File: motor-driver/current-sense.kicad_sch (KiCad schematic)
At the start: 49 parts, among them U1 LM358DR, U2 LM358DR, U3 LM358DR, U4 LM358DR, U5 LM358DR

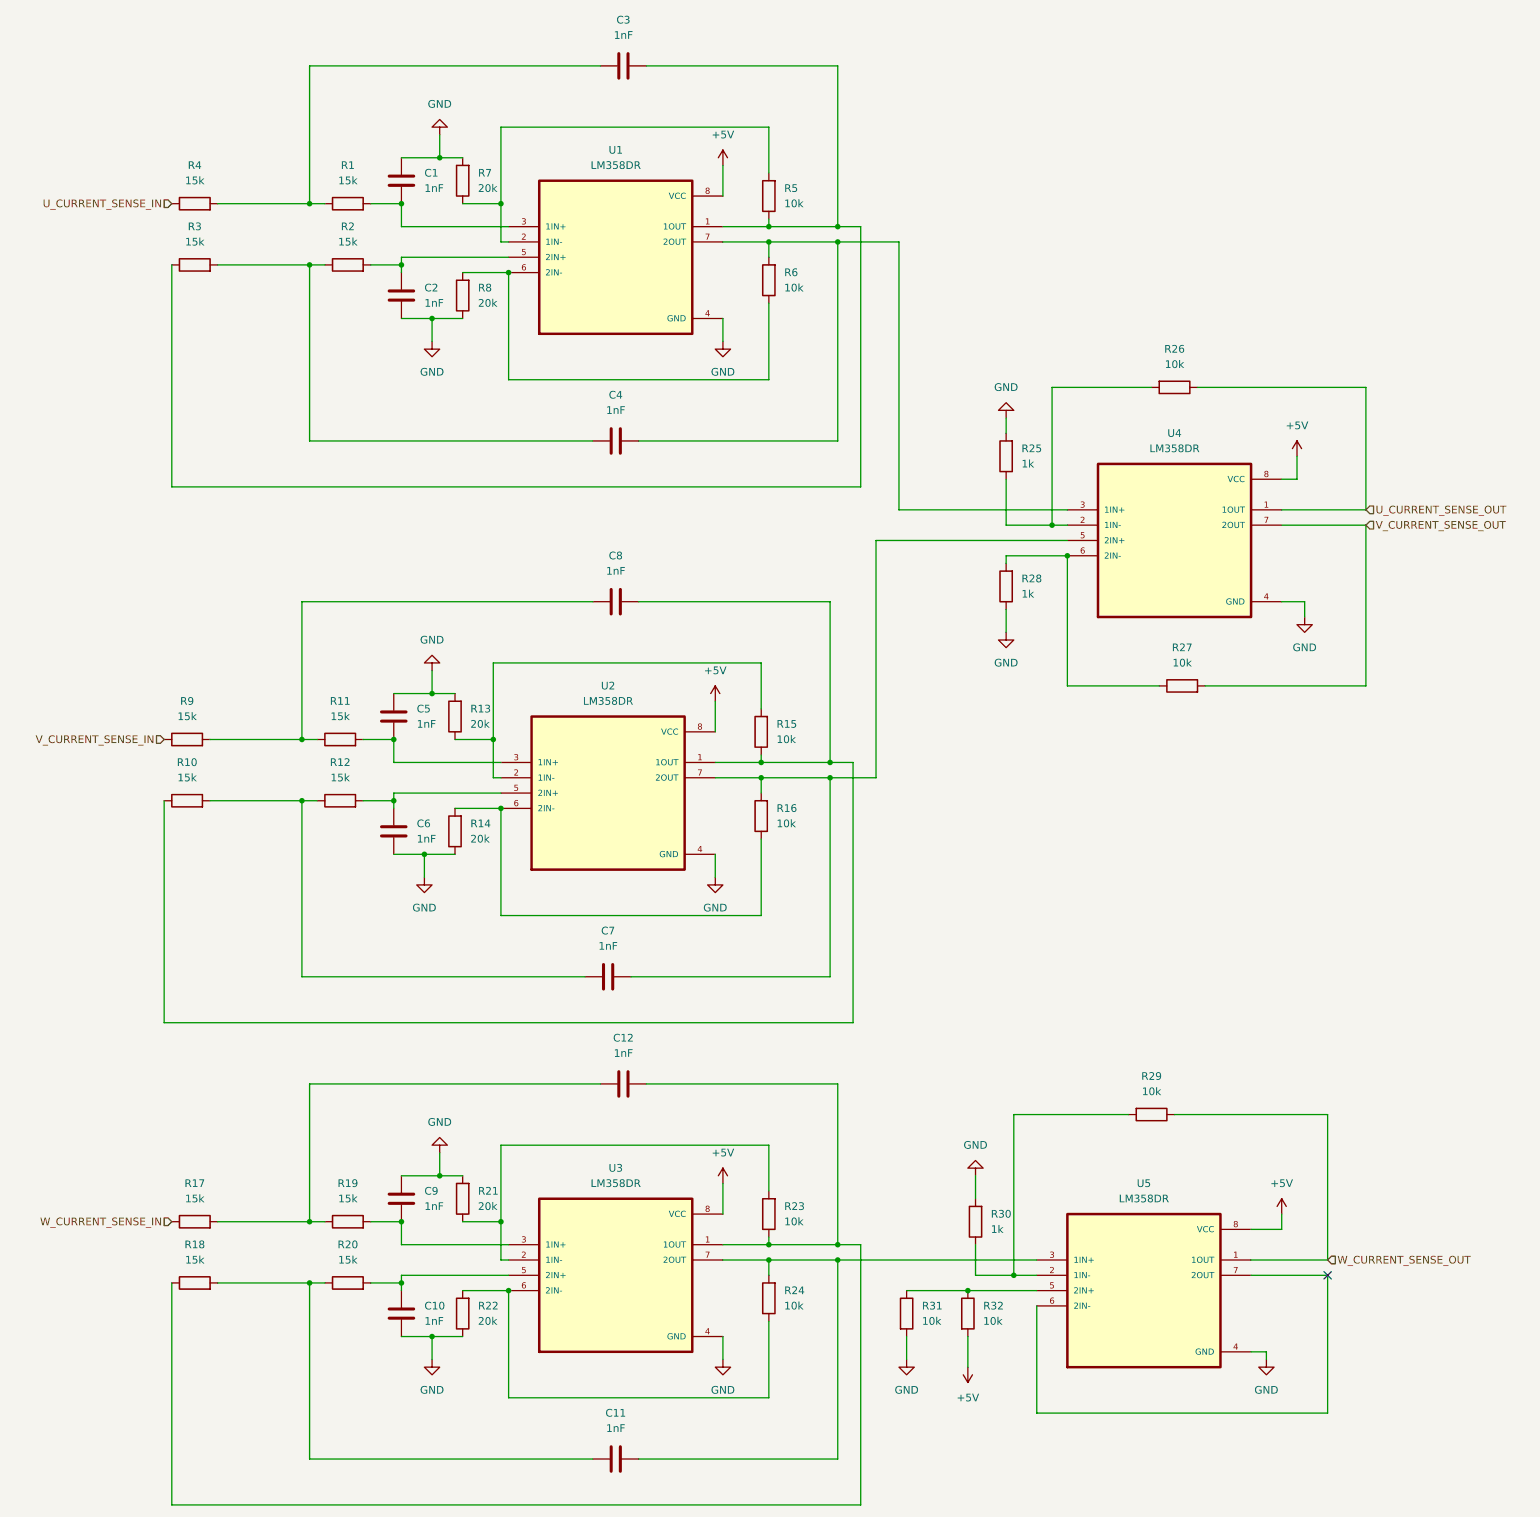
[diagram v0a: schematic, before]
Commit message: completed sheet connections
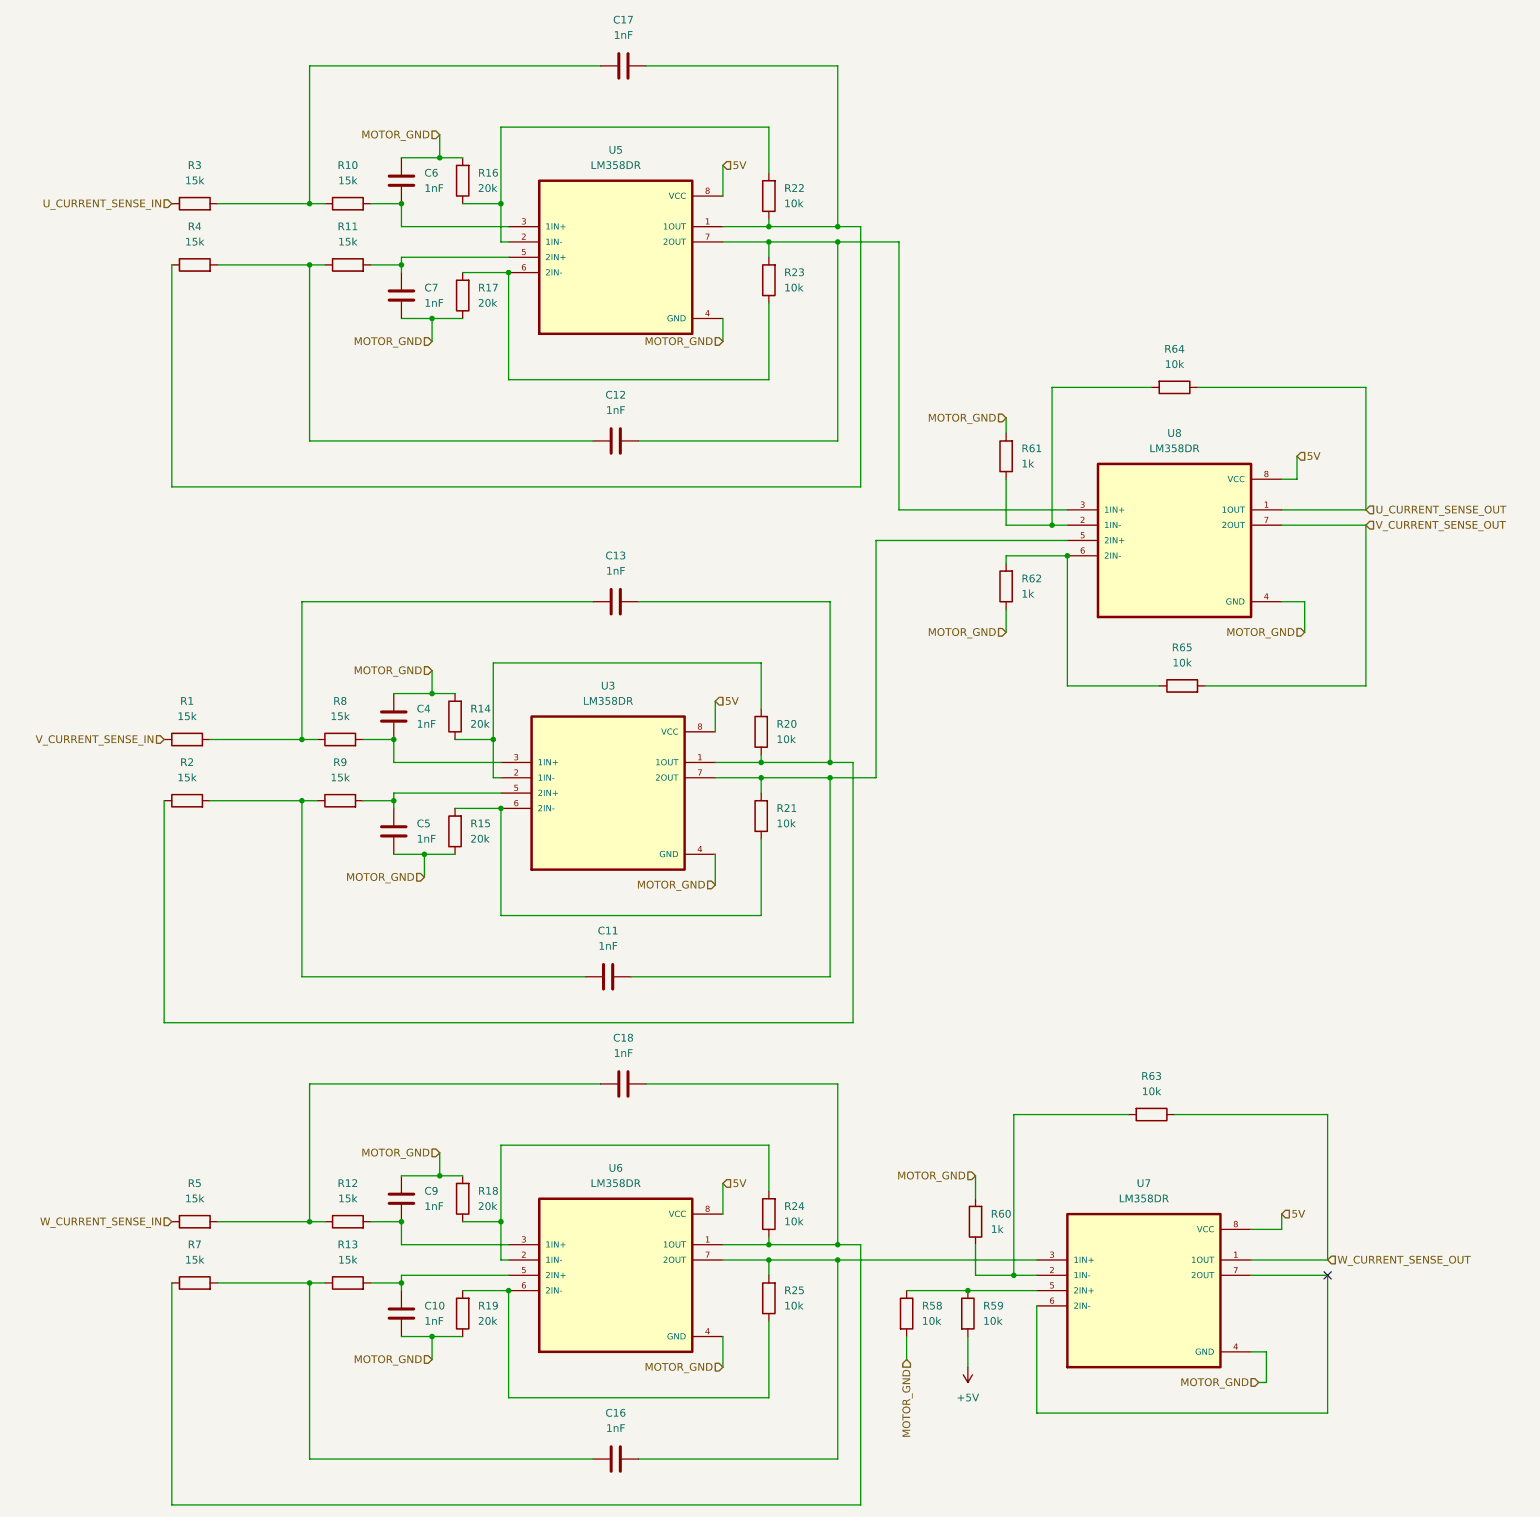
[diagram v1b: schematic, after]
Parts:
- renumbered C7 to C11, C4 to C12, C8 to C13, C11 to C16, C3 to C17, C12 to C18, C5 to C4, C6 to C5, C1 to C6, C2 to C7, R9 to R1, R1 to R10, R2 to R11, R19 to R12, R20 to R13, R13 to R14, R14 to R15, R7 to R16, R8 to R17, R21 to R18, R22 to R19, R10 to R2, R15 to R20, R16 to R21, R5 to R22, R6 to R23, R23 to R24, R24 to R25, R4 to R3, R3 to R4, R17 to R5, R31 to R58, R32 to R59, R30 to R60, R25 to R61, R28 to R62, R29 to R63, R26 to R64, R27 to R65, R18 to R7, R11 to R8, R12 to R9, U2 to U3, U1 to U5, U3 to U6, U5 to U7, U4 to U8
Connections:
- net +5V: no longer U3.8 (VCC), U5.8 (VCC), U6.8 (VCC), U7.8 (VCC), U8.8 (VCC)
- net GND renamed MOTOR_GND
- new net 5V: U3.8 (VCC), U5.8 (VCC), U6.8 (VCC), U7.8 (VCC), U8.8 (VCC)

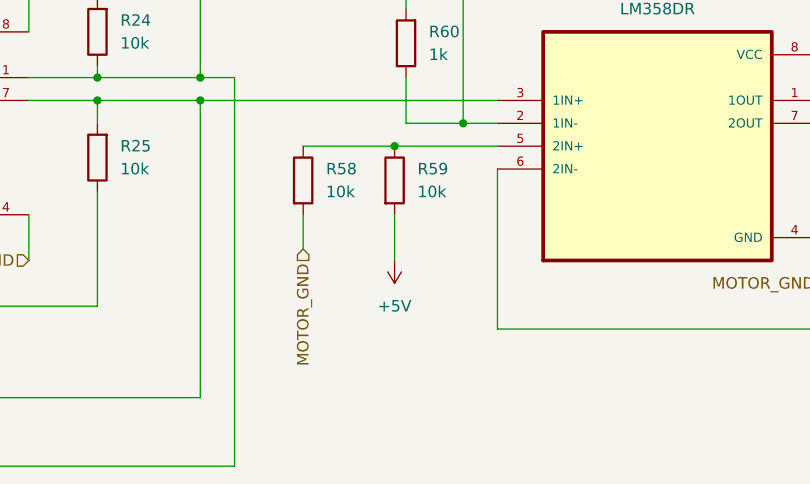
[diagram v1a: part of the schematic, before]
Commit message: added connectors starting pcb layout
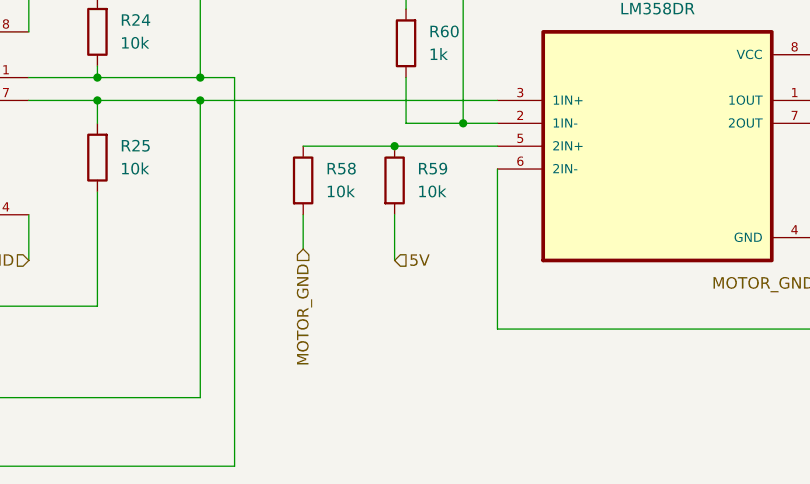
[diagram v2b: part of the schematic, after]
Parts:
- C10, C11, C12, C13, C16, C17, C18, C4, C5, C6, C7, C9: footprint (none) -> Capacitor_SMD:C_0805_2012Metric
- R1, R10, R11, R12, R13, R14, R15, R16, R17, R18, R19, R2, R20, R21, R22, R23, R24, R25, R3, R4, R5, R58, R59, R60, R61, R62, R63, R64, R65, R7, R8, R9: footprint (none) -> Resistor_SMD:R_0805_2012Metric
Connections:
- net +5V is gone; now on net 5V: R59.2
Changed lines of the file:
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@@
 		)
 	)
+	(hierarchical_label "5V"
+		(shape input)
+		(at 176.53 237.49 0)
+		(effects
+			(font
+				(size 1.27 1.27)
+			)
+			(justify left)
+		)
+	)
 	(hierarchical_label "MOTOR_GND"
 		(shape input)
@@
 			)
 		)
-		(property "Footprint" ""
+		(property "Footprint" "Resistor_SMD:R_0805_2012Metric"
 			(at 94.488 40.64 90)
 			(effects
@@
 			)
 		)
-		(property "Footprint" ""
+		(property "Footprint" "Resistor_SMD:R_0805_2012Metric"
 			(at 174.752 228.6 90)
 			(effects
@@
 			)
 		)
-		(property "Footprint" ""
+		(property "Footprint" "Resistor_SMD:R_0805_2012Metric"
 			(at 46.99 145.288 90)
 			(effects
@@
 			)
 		)
-		(property "Footprint" ""
+		(property "Footprint" "Capacitor_SMD:C_0805_2012Metric"
 			(at 115.57 22.5552 0)
 			(effects
@@
 			)
 		)
-		(property "Footprint" ""
+		(property "Footprint" "Resistor_SMD:R_0805_2012Metric"
 			(at 145.288 212.09 90)
 			(effects
@@
 			)
 		)
-		(property "Footprint" ""
+		(property "Footprint" "Capacitor_SMD:C_0805_2012Metric"
 			(at 114.3 111.4552 0)
 			(effects
@@
 			)
 		)
-		(property "Footprint" ""
+		(property "Footprint" "Resistor_SMD:R_0805_2012Metric"
 			(at 145.288 43.18 90)
 			(effects
@@
 			)
 		)
-		(property "Footprint" ""
+		(property "Footprint" "Resistor_SMD:R_0805_2012Metric"
 			(at 164.592 228.6 90)
 			(effects
@@
 			)
 		)
-		(property "Footprint" ""
+		(property "Footprint" "Capacitor_SMD:C_0805_2012Metric"
 			(at 81.5848 55.88 0)
 			(effects
@@
 			)
 		)
-		(property "Footprint" ""
+		(property "Footprint" "Capacitor_SMD:C_0805_2012Metric"
 			(at 80.3148 144.78 0)
 			(effects
@@
 			)
 		)
-		(property "Footprint" ""
+		(property "Footprint" "Resistor_SMD:R_0805_2012Metric"
 			(at 145.288 57.15 90)
 			(effects
@@
 			)
 		)
-		(property "Footprint" ""
+		(property "Footprint" "Resistor_SMD:R_0805_2012Metric"
 			(at 73.66 46.228 90)
 			(effects
@@
 			)
 		)
-		(property "Footprint" ""
+		(property "Footprint" "Capacitor_SMD:C_0805_2012Metric"
 			(at 81.5848 205.74 0)
 			(effects
@@
 			)
 		)
-		(property "Footprint" ""
+		(property "Footprint" "Resistor_SMD:R_0805_2012Metric"
 			(at 48.26 215.138 90)
 			(effects
@@
 			)
 		)
-		(property "Footprint" ""
+		(property "Footprint" "Resistor_SMD:R_0805_2012Metric"
 			(at 210.82 73.152 90)
 			(effects
@@
 			)
 		)
-		(property "Footprint" ""
+		(property "Footprint" "Resistor_SMD:R_0805_2012Metric"
 			(at 46.99 135.128 90)
 			(effects
@@
 			)
 		)
-		(property "Footprint" ""
+		(property "Footprint" "Resistor_SMD:R_0805_2012Metric"
 			(at 73.66 215.138 90)
 			(effects
@@
 			)
 		)
-		(property "Footprint" ""
+		(property "Footprint" "Resistor_SMD:R_0805_2012Metric"
 			(at 48.26 56.388 90)
 			(effects
@@
 			)
 		)
-		(property "Footprint" ""
+		(property "Footprint" "Capacitor_SMD:C_0805_2012Metric"
 			(at 114.3 253.6952 0)
 			(effects
@@
 			)
 		)
-		(property "Footprint" ""
+		(property "Footprint" "Resistor_SMD:R_0805_2012Metric"
 			(at 94.488 228.6 90)
 			(effects
@@
 			)
 		)
-		(property "Footprint" ""
+		(property "Footprint" "Capacitor_SMD:C_0805_2012Metric"
 			(at 115.57 191.4652 0)
 			(effects
@@
 			)
 		)
-		(property "Footprint" ""
+		(property "Footprint" "Resistor_SMD:R_0805_2012Metric"
 			(at 207.01 193.802 90)
 			(effects
@@
 			)
 		)
-		(property "Footprint" ""
+		(property "Footprint" "Capacitor_SMD:C_0805_2012Metric"
 			(at 81.5848 224.79 0)
 			(effects
@@
 			)
 		)
-		(property "Footprint" ""
+		(property "Footprint" "Capacitor_SMD:C_0805_2012Metric"
 			(at 114.3 84.7852 0)
 			(effects
@@
 			)
 		)
-		(property "Footprint" ""
+		(property "Footprint" "Resistor_SMD:R_0805_2012Metric"
 			(at 48.26 225.298 90)
 			(effects
@@
 			)
 		)
-		(property "Footprint" ""
+		(property "Footprint" "Resistor_SMD:R_0805_2012Metric"
 			(at 145.288 226.06 90)
 			(effects
@@
 			)
 		)
-		(property "Footprint" ""
+		(property "Footprint" "Resistor_SMD:R_0805_2012Metric"
 			(at 48.26 46.228 90)
 			(effects
@@
 			)
 		)
-		(property "Footprint" ""
+		(property "Footprint" "Resistor_SMD:R_0805_2012Metric"
 			(at 94.488 59.69 90)
 			(effects
@@
 			)
 		)
-		(property "Footprint" ""
+		(property "Footprint" "Resistor_SMD:R_0805_2012Metric"
 			(at 93.218 129.54 90)
 			(effects
@@
 	)
 	(symbol
-		(lib_id "power:+5V")
-		(at 176.53 237.49 180)
-		(unit 1)
-		(exclude_from_sim no)
-		(in_bom yes)
-		(on_board yes)
-		(dnp no)
-		(fields_autoplaced yes)
-		(property "Reference" "#PWR014"
-			(at 176.53 233.68 0)
-			(effects
-				(font
-					(size 1.27 1.27)
-				)
-				(hide yes)
-			)
-		)
-		(property "Value" "+5V"
-			(at 176.53 242.57 0)
-			(effects
-				(font
-					(size 1.27 1.27)
-				)
-			)
-		)
-		(property "Footprint" ""
-			(at 176.53 237.49 0)
-			(effects
-				(font
-					(size 1.27 1.27)
-				)
-				(hide yes)
-			)
-		)
-		(property "Datasheet" ""
-			(at 176.53 237.49 0)
-			(effects
-				(font
-					(size 1.27 1.27)
-				)
-				(hide yes)
-			)
-		)
-		(property "Description" "Power symbol creates a global label with name \"+5V\""
-			(at 176.53 237.49 0)
-			(effects
-				(font
-					(size 1.27 1.27)
-				)
-				(hide yes)
-			)
-		)
-		(pin "1"
-		)
-		(instances
-			(project "current-sense"
-				(path "/14b53516-7ab2-47c8-8e94-c5beb6fd44de"
-					(reference "#PWR021")
-					(unit 1)
-				)
-			)
-			(project "motor-driver"
-				(path "/2980fc7e-b297-4843-ba9f-cceafa384b2f/5c70832b-4bf7-4293-9eac-400db3aae7be"
-					(reference "#PWR014")
-					(unit 1)
-				)
-			)
-		)
-	)
-	(symbol
 		(lib_id "LM358DR:LM358DR")
 		(at 116.84 142.24 0)
@@
 			)
 		)
-		(property "Footprint" ""
+		(property "Footprint" "Resistor_SMD:R_0805_2012Metric"
 			(at 73.66 225.298 90)
 			(effects
@@
 			)
 		)
-		(property "Footprint" ""
+		(property "Footprint" "Capacitor_SMD:C_0805_2012Metric"
 			(at 80.3148 125.73 0)
 			(effects
@@
 			)
 		)
-		(property "Footprint" ""
+		(property "Footprint" "Capacitor_SMD:C_0805_2012Metric"
 			(at 113.03 173.6852 0)
 			(effects
@@
 			)
 		)
-		(property "Footprint" ""
+		(property "Footprint" "Resistor_SMD:R_0805_2012Metric"
 			(at 72.39 145.288 90)
 			(effects
@@
 			)
 		)
-		(property "Footprint" ""
+		(property "Footprint" "Resistor_SMD:R_0805_2012Metric"
 			(at 93.218 148.59 90)
 			(effects
@@
 			)
 		)
-		(property "Footprint" ""
+		(property "Footprint" "Resistor_SMD:R_0805_2012Metric"
 			(at 94.488 209.55 90)
 			(effects
@@
 			)
 		)
-		(property "Footprint" ""
+		(property "Footprint" "Resistor_SMD:R_0805_2012Metric"
 			(at 179.578 213.36 90)
 			(effects
@@
 			)
 		)
-		(property "Footprint" ""
+		(property "Footprint" "Capacitor_SMD:C_0805_2012Metric"
 			(at 81.5848 36.83 0)
 			(effects
@@
 			)
 		)
-		(property "Footprint" ""
+		(property "Footprint" "Resistor_SMD:R_0805_2012Metric"
 			(at 144.018 132.08 90)
 			(effects
@@
 			)
 		)
-		(property "Footprint" ""
+		(property "Footprint" "Resistor_SMD:R_0805_2012Metric"
 			(at 144.018 146.05 90)
 			(effects
@@
 			)
 		)
-		(property "Footprint" ""
+		(property "Footprint" "Resistor_SMD:R_0805_2012Metric"
 			(at 184.658 107.95 90)
 			(effects
@@
 			)
 		)
-		(property "Footprint" ""
+		(property "Footprint" "Resistor_SMD:R_0805_2012Metric"
 			(at 72.39 135.128 90)
 			(effects
@@
 			)
 		)
-		(property "Footprint" ""
+		(property "Footprint" "Resistor_SMD:R_0805_2012Metric"
 			(at 184.658 86.36 90)
 			(effects
@@
 			)
 		)
-		(property "Footprint" ""
+		(property "Footprint" "Resistor_SMD:R_0805_2012Metric"
 			(at 73.66 56.388 90)
 			(effects
@@
 			)
 		)
-		(property "Footprint" ""
+		(property "Footprint" "Resistor_SMD:R_0805_2012Metric"
 			(at 212.09 126.238 90)
 			(effects
